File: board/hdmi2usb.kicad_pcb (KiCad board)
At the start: 8 copper layers, 180.3 x 101 mm, 446 parts, among them J1 USB_MICRO_B, J2 HDMI, J3 HDMI, J4 HDMI, J5 DVI-STACKED, J6 DVI-STACKED, J7 HDMI, J8 VHDCI, J9 DVI-STACKED, P1 CONN_7X2, P10 CONN_1, P11 CONN_1, P12 CONN_1, P13 CONN_1, P14 CONN_1, P15 CONN_1, P16 CONN_1, P17 CONN_1, P18 CONN_1, P19 CONN_1, P2 CONN_1, P20 CONN_1, P21 CONN_1, P22 CONN_1, P23 CONN_1, P24 CONN_1, P25 CONN_1, P26 CONN_1, P27 CONN_1, P28 CONN_1, P29 CONN_1, P3 CONN_1, P30 CONN_1, P31 CONN_1, P32 CONN_1, P33 CONN_1, P34 CONN_1, P35 CONN_1, P36 CONN_1, P37 CONN_1, P38 CONN_1, P39 CONN_1, P4 CONN_1, P40 CONN_1, P41 CONN_1, P42 CONN_1, P43 CONN_1, P44 CONN_1, P45 CONN_1, P46 CONN_1, P5 CONN_1, P6 CONN_1, P7 CONN_1, P8 CONN_1, P9 CONN_1, U1 CY7C68013A, U10 IP4776CZ38, U11 IP4776CZ38, U12 SPARTAN6LXXXX-CSG324, U13 FXO-HC536R, U2 M25P16, U3 LMR10530, U4 LMR10530, U5 LMR10530, U6 LP2997, U7 MT47H64M16HR, U8 IP4776CZ38, U9 IP4776CZ38, X1 CRYSTAL

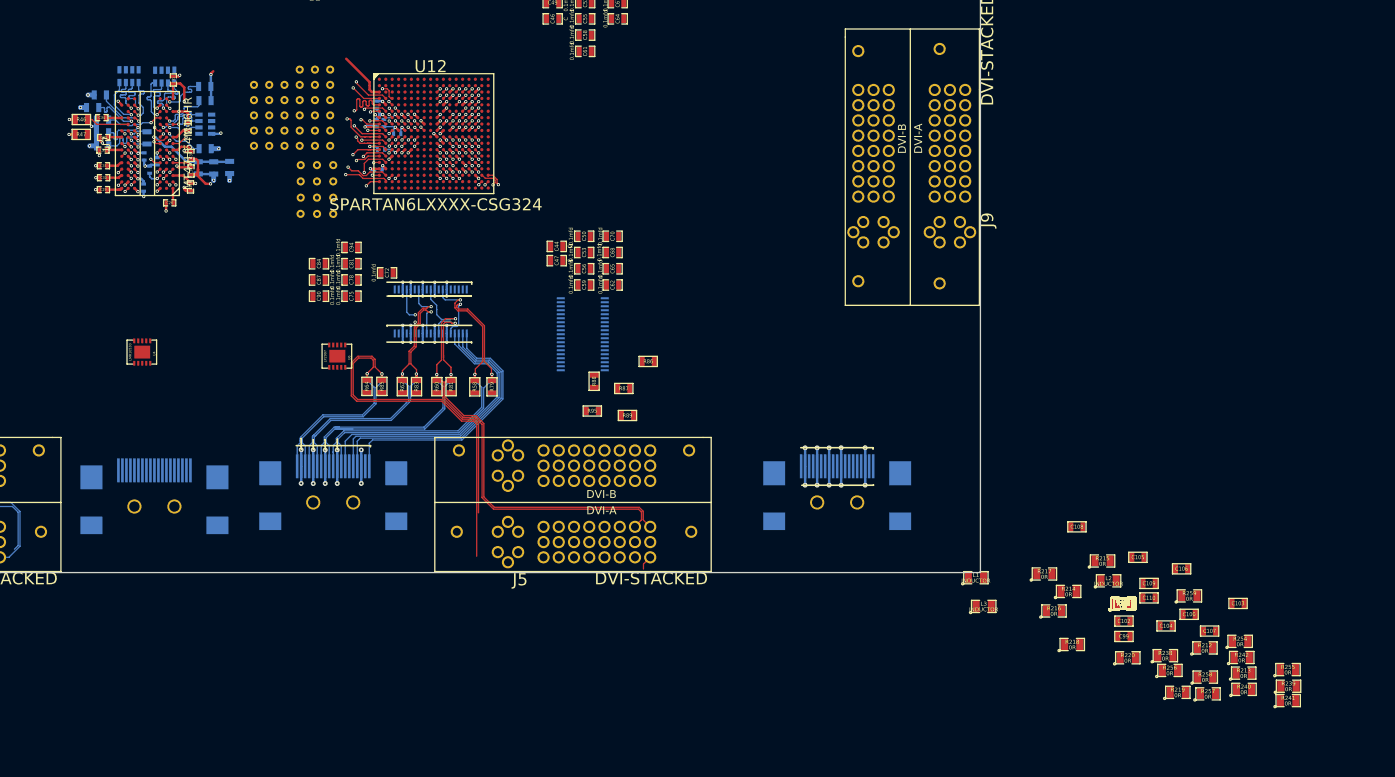
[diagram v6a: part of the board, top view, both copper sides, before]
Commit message: Issue #606 - Length matching od DDR signals are finished.
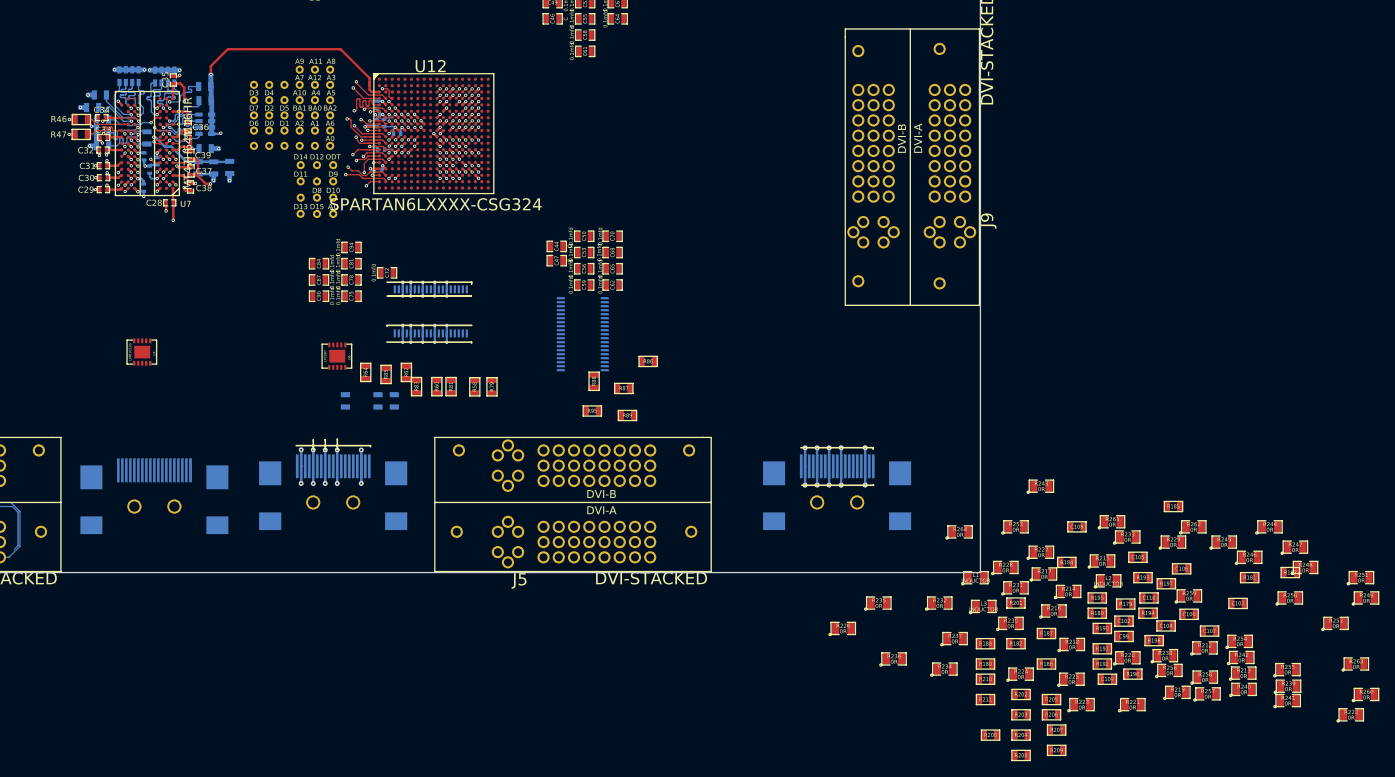
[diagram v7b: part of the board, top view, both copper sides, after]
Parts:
- R177, R178, R199: moved to B.Cu
- moved R177 100.5 mm to (221.0, 190.0), turned to 270 degrees
- moved R178 96.6 mm to (225.0, 190.0), turned to 270 degrees
- moved R199 94.6 mm to (227.1, 190.0), turned to 270 degrees
- moved R226 35.1 mm to (283.2, 218.4)
- moved R260 32.5 mm to (348.6, 226.7)
- moved R222 31.7 mm to (346.7, 229.2)
- moved R235 30.6 mm to (287.7, 215.3)
- moved R249 30.4 mm to (348.6, 214.6)
- moved R263 30.1 mm to (347.3, 222.9)
- moved R251 29.9 mm to (348.0, 212.1)
- moved R236 29.5 mm to (289.6, 222.2)
- moved R252 26.7 mm to (344.8, 217.8)
- moved R234 23.8 mm to (295.9, 223.5)
- moved R200 23.3 mm to (301.6, 231.8)
- moved R248 23.2 mm to (341.0, 210.8)
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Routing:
- net /hdmi/TMDS-RX1-1_P: track 124.7 -> 0.00 mm, vias 3 -> 0
- net /hdmi/TMDS-RX1-1_N: track 122.0 -> 0.00 mm, vias 3 -> 0
- net /hdmi/TMDS-RX1-CLK_P: track 102.8 -> 0.00 mm, vias 3 -> 0
- net /hdmi/TMDS-RX1-0_P: track 99.4 -> 0.00 mm, vias 3 -> 0
- net /hdmi/TMDS-RX1-2_N: track 99.2 -> 0.00 mm, vias 3 -> 0
- net /hdmi/TMDS-RX1-0_N: track 97.8 -> 0.00 mm, vias 3 -> 0
- net /hdmi/TMDS-RX1-2_P: track 94.1 -> 0.00 mm, vias 3 -> 0
- net /hdmi/TMDS-RX1-CLK_N: track 90.0 -> 0.00 mm, vias 3 -> 0
- net /hdmi/P1-CEC: track 35.5 -> 0.00 mm
- net /hdmi/P1-SCL: track 31.5 -> 0.00 mm
- net /hdmi/P1-SDA: track 31.3 -> 0.00 mm
- net DDR0V9: track 22.4 -> 53.4 mm, vias 8 -> 12
- net /hdmi/P1-HOT: track 30.1 -> 0.00 mm
- net N-00000449: track 13.5 -> 0.00 mm
- net /MT47H64M16HR/DDR-WE: track 36.1 -> 48.4 mm
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- added copper zone on PWR, net DDR0V9
- added copper zone on PWR, net DDR1V8
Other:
- board text added: "A0"
- board text added: "A1"
- board text added: "A10"
- board text added: "A11"
- board text added: "A12"
- board text added: "A2"
- board text added: "A3"
- board text added: "A4"
- board text added: "A5"
- board text added: "A6"
- board text added: "A7"
- board text added: "A8"
- board text added: "A9"
- board text added: "BA0"
- board text added: "BA1"
- board text added: "BA2"
- board text added: "CAS"
- board text added: "CKE"
- board text added: "CKN"
- board text added: "CKP"
- board text added: "D0"
- board text added: "D1"
- board text added: "D10"
- board text added: "D11"
- board text added: "D12"
- board text added: "D13"
- board text added: "D14"
- board text added: "D15"
- board text added: "D2"
- board text added: "D3"
- board text added: "D4"
- board text added: "D5"
- board text added: "D6"
- board text added: "D7"
- board text added: "D8"
- board text added: "D9"
- board text added: "LDM"
- board text added: "LDQS_N"
- board text added: "LDQS_P"
- board text added: "ODT"
- board text added: "RAS"
- board text added: "UDM"
- board text added: "UDQS_N"
- board text added: "UDQS_P"
- board text added: "WE"

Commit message: Issue #859 - Changes as per the review
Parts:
- added C111: 0.1mfd, SM0402_c, B.Cu at (225.5, 159.8)
- added C112: 0.1mfd, SM0402_c, B.Cu at (223.4, 149.9)
- added C27: 0.1mfd, SM0402_c, B.Cu at (227.7, 159.7)
- moved C89 1.38 mm to (224.9, 156.7), turned to 180 degrees
- moved C101 0.54 mm to (225.2, 155.3), turned to 180 degrees
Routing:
- net DDR0V9: track 53.4 -> 76.1 mm, vias 12 -> 13
- net DDR1V8: track 62.3 -> 60.1 mm
- net GND: track 81.2 -> 83.1 mm, vias 74 -> 75
